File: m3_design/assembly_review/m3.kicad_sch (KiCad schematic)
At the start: 15 parts, among them J3 USB-C 2.0, U2 AP63203WU-7

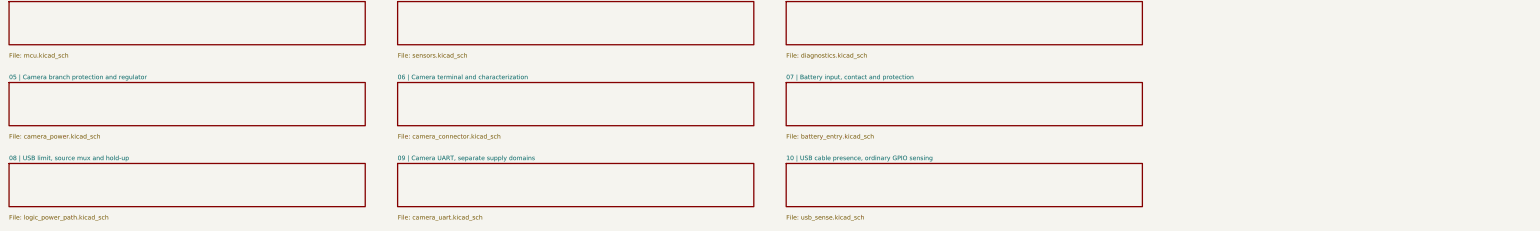
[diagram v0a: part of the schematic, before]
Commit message: M3-ASSY-R2: merge servos, dual fused pyro, arming, pull-pin and buzzer
Adds every remaining hardware function to the single M3 board (46 x 238 mm,
203 positions / 178 fitted parts, 14 sheets):

- Actuator power switch: back-to-back AON6403 from the battery input, gated
  by the U9 logic path so the one external switch still controls everything.
- Single-deploy dual pyro (owner ruling 2026-09-25): two AON7524 channels on
  two independently fused buses (FMEA H-5), separate 4-pos ARM and igniter
  terminals, per-bus arm sense, continuity, cold pull-up (H-1), gate networks
  per MARGIN_PRESCRIPTION P0-1/P0-2, PE3/PE6 sentinels (LED_RED -> PE8).
- Four servos (1 k series, pull-downs, SRV05-4), clamped pull-pin (PC14),
  MLT-8530 buzzer (PA5; pad mapping from the maker spec).
- Backup altimeter fully isolated by ruling: no interface on the board.
- New AON7524 footprint from AOS PO-00047 rev I; U12 LCSC code added.
- tools/export_fab.py (Gerber/drill zip, JLC BOM + CPL); m3_design/
  check_actuators.py (arming break / gate-network contract from PCB nets).

CAD checks only: tools/check.sh DRC 0 / unconnected 0 / parity 0 / ERC 0,
audit OK. No bench, simulation or flight evidence; no R2 firmware yet.

Co-Authored-By: Claude Opus 5.5 <noreply@anthropic.com>
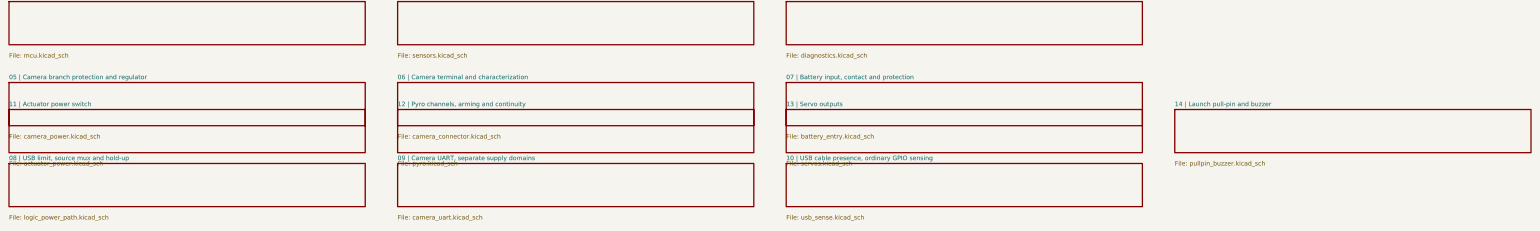
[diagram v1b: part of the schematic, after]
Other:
- added sheet 11 | Actuator power switch (actuator_power.kicad_sch)
- added sheet 12 | Pyro channels, arming and continuity (pyro.kicad_sch)
- added sheet 13 | Servo outputs (servos.kicad_sch)
- added sheet 14 | Launch pull-pin and buzzer (pullpin_buzzer.kicad_sch)
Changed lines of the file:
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@@
 			(justify left))
 )
+	(sheet
+		(at 20.32 256.54)
+		(size 83.82 10.16)
+		(stroke
+			(width .254)
+			(type default))
+		(fill
+			(color 0 0 0 0))
+		(property "Sheetname" "11 | Actuator power switch"
+			(at 20.32 255.27 0)
+			(effects
+				(font
+					(size 1.05 1.05))
+				(justify left)))
+		(property "Sheetfile" "actuator_power.kicad_sch"
+			(at 20.32 269.24 0)
+			(effects
+				(font
+					(size 1.05 1.05))
+				(justify left)))
+		(instances
+			(project "m3"
+				(path "/6007a7db-6a58-5660-8beb-956dea045ff8"
+					(page "11")))))
+	(sheet
+		(at 111.76 256.54)
+		(size 83.82 10.16)
+		(stroke
+			(width .254)
+			(type default))
+		(fill
+			(color 0 0 0 0))
+		(property "Sheetname" "12 | Pyro channels, arming and continuity"
+			(at 111.76 255.27 0)
+			(effects
+				(font
+					(size 1.05 1.05))
+				(justify left)))
+		(property "Sheetfile" "pyro.kicad_sch"
+			(at 111.76 269.24 0)
+			(effects
+				(font
+					(size 1.05 1.05))
+				(justify left)))
+		(instances
+			(project "m3"
+				(path "/6007a7db-6a58-5660-8beb-956dea045ff8"
+					(page "12")))))
+	(sheet
+		(at 203.2 256.54)
+		(size 83.82 10.16)
+		(stroke
+			(width .254)
+			(type default))
+		(fill
+			(color 0 0 0 0))
+		(property "Sheetname" "13 | Servo outputs"
+			(at 203.2 255.27 0)
+			(effects
+				(font
+					(size 1.05 1.05))
+				(justify left)))
+		(property "Sheetfile" "servos.kicad_sch"
+			(at 203.2 269.24 0)
+			(effects
+				(font
+					(size 1.05 1.05))
+				(justify left)))
+		(instances
+			(project "m3"
+				(path "/6007a7db-6a58-5660-8beb-956dea045ff8"
+					(page "13")))))
+	(sheet
+		(at 294.64 256.54)
+		(size 83.82 10.16)
+		(stroke
+			(width .254)
+			(type default))
+		(fill
+			(color 0 0 0 0))
+		(property "Sheetname" "14 | Launch pull-pin and buzzer"
+			(at 294.64 255.27 0)
+			(effects
+				(font
+					(size 1.05 1.05))
+				(justify left)))
+		(property "Sheetfile" "pullpin_buzzer.kicad_sch"
+			(at 294.64 269.24 0)
+			(effects
+				(font
+					(size 1.05 1.05))
+				(justify left)))
+		(instances
+			(project "m3"
+				(path "/6007a7db-6a58-5660-8beb-956dea045ff8"
+					(page "14")))))
 	(sheet_instances
 		(path "/"

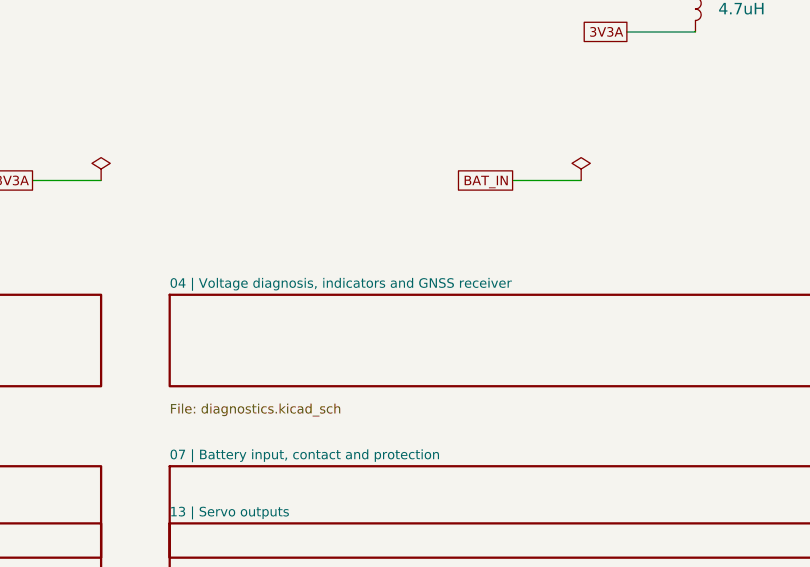
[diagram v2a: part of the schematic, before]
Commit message: M3-ASSY-R3: remove GNSS, cut board to 46 x 193 mm
Schematic: U6/C33/C34 and GPS_TX/GPS_RX removed, PC6/PC7 no-connect, sheet 04
renamed, title-block revision R3 on all 14 sheets. PCB: m3_design/r3_cut.py deletes
227 tracks/vias (GPS nets, the U6-only 3V3A branch, forward GND stitching) and
U6/C33/C34; outline 46 x 193 mm, forward M3 pair moved to y = 189, GND zones
trimmed and refilled. No remaining track, via or footprint moved (checked
against R2). check.sh: DRC 0, unconnected 0, parity 0, ERC 0, audit OK;
check_actuators OK. Sheets, netlist, DRC/ERC evidence and renders regenerated.

Co-Authored-By: Claude Opus 5.5 <noreply@anthropic.com>
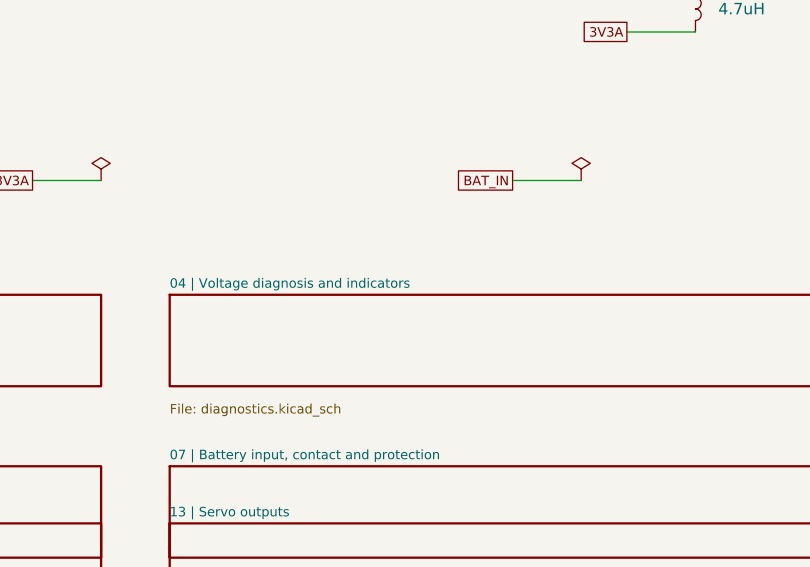
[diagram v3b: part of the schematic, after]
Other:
- sheet 04 | Voltage diagnosis, indicators and GNSS receiver renamed 04 | Voltage diagnosis and indicators
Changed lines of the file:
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@@
 		(title "01 | USB input and regulated supplies")
 		(date "2026-09-07")
-		(rev "M3-ASSY-R1")
+		(rev "M3-ASSY-R3")
 		(company "Single-board M3 candidate; full system incomplete"))
 	(text "01 | USB input and regulated supplies"
@@
 		(fill
 			(color 0 0 0 0))
-		(property "Sheetname" "04 | Voltage diagnosis, indicators and GNSS receiver"
+		(property "Sheetname" "04 | Voltage diagnosis and indicators"
 			(at 203.2 229.86999999999998 0)
 			(effects

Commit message: M3-ASSY-R4: R3 validation fixes, new IMU, fault-tolerant pyro sensing
The board, schematic sheets and footprint library are generated from
R3 (533af8e) by m3_design/r4_build.sh (r4_lib.py, r4_sch.py,
r4_pcb.py). docs/REQUIREMENTS.md states what the board must do;
docs/M3_R4.md records every change, the thirteen evaluation passes
(twelve independent reviews) and the accepted deviations.

- IMU: ST LSM6DSV320X (16 g and 320 g, 4000 dps)
- Pyro: black ARM and orange igniter terminals, eight pyro spacing
  rules in m3.kicad_dru, sense dividers of 2 x 5.1k over 2 x 2k in
  parallel, 4.7k at each ADC pin (R168-R172)
- Pull-pin on a JST PH connector; JLC tooling holes
- Fab: Standard PCBA, 84 BOM lines, 205 placed parts, $80.12 per board
  at five boards (tools/jlc_cost.py); placement rotations verified
- Gate: tools/check.sh DRC 0, unconnected 0, schematic parity 0, ERC 0,
  audit OK; m3_design/check_actuators.py OK

Nothing has been built or measured, and there is no R4 firmware. The
open owner decisions and the bench tests are listed in STATUS.md.

Co-Authored-By: Claude Opus 5.5 <noreply@anthropic.com>
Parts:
- R164: renamed from L2; value 4.7uH -> 2.2R 1%; footprint rocket:IND-SMD_L4.0-W4.0 -> rocket:R_0603_1608Metric; symbol M3:L -> M3:R; LCSC C57269 -> C22939
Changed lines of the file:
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@@
 		(title "01 | USB input and regulated supplies")
 		(date "2026-09-07")
-		(rev "M3-ASSY-R3")
+		(rev "M3-ASSY-R4")
 		(company "Single-board M3 candidate; full system incomplete"))
 	(text "01 | USB input and regulated supplies"
@@
 )
 	(symbol
-		(lib_id "M3:L")
+		(lib_id "M3:R")
 		(at 261.62 198.12 0)
 		(unit 1)
@@
 		(on_board yes)
 		(dnp no)
-		(property "Reference" "L2"
+		(property "Reference" "R164"
 			(at 264.16 196.85 0)
 			(effects
@@
 					(size 1.27 1.27))
 				(justify left)))
-		(property "Value" "4.7uH"
+		(property "Value" "2.2R 1%"
 			(at 264.16 199.39 0)
 			(effects
@@
 					(size 1.27 1.27))
 				(justify left)))
-		(property "Footprint" "rocket:IND-SMD_L4.0-W4.0"
+		(property "Footprint" "rocket:R_0603_1608Metric"
 			(at 261.62 198.12 0)
 			(hide yes)
@@
 					(size 1.27 1.27))
 				(justify left)))
-		(property "LCSC" "C57269"
+		(property "LCSC" "C22939"
 			(at 261.62 198.12 0)
 			(hide yes)
@@
 			(project "m3"
 				(path "/6007a7db-6a58-5660-8beb-956dea045ff8"
-					(reference "L2")
+					(reference "R164")
 					(unit 1)))))
 	(wire
